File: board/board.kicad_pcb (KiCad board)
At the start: 2 copper layers, 58.1 x 29.5 mm, 41 parts, among them J2 Conn_01x10, J3 Conn_01x06, J4 Conn_01x02, J7 Conn_01x30, J8 USB_C_Receptacle_USB2.0_16P, J9 Conn_01x02, U2 nPM1300-QEAA, U3 MDBT50Q-P1MV2, U4 TVS_Array, Y1 32k Hz

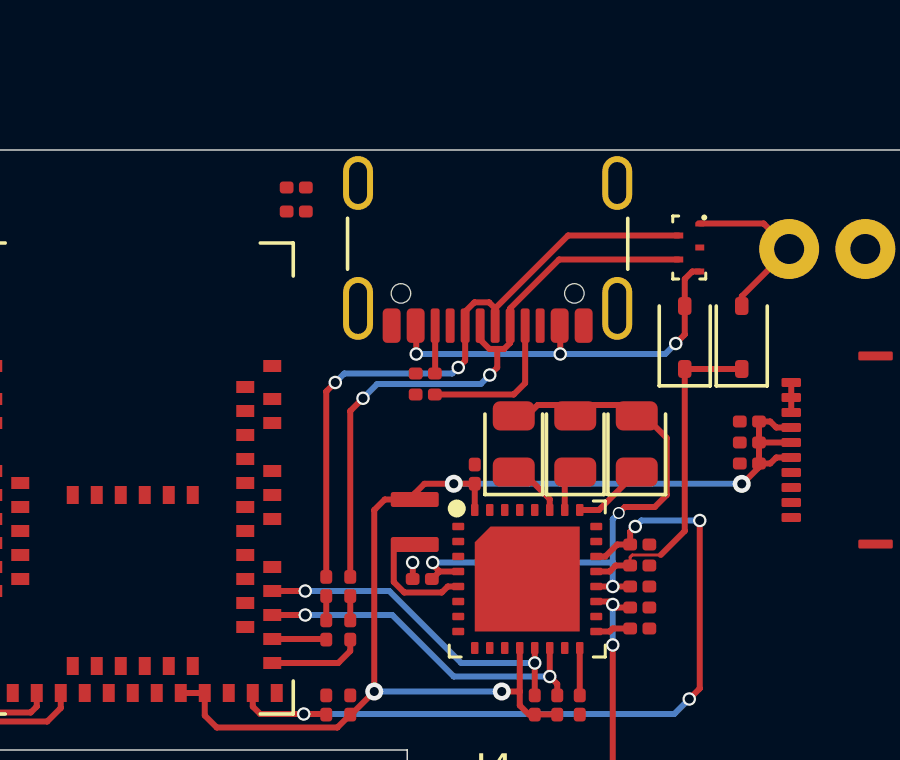
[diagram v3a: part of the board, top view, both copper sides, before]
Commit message: board: pcb add usb shield grounding
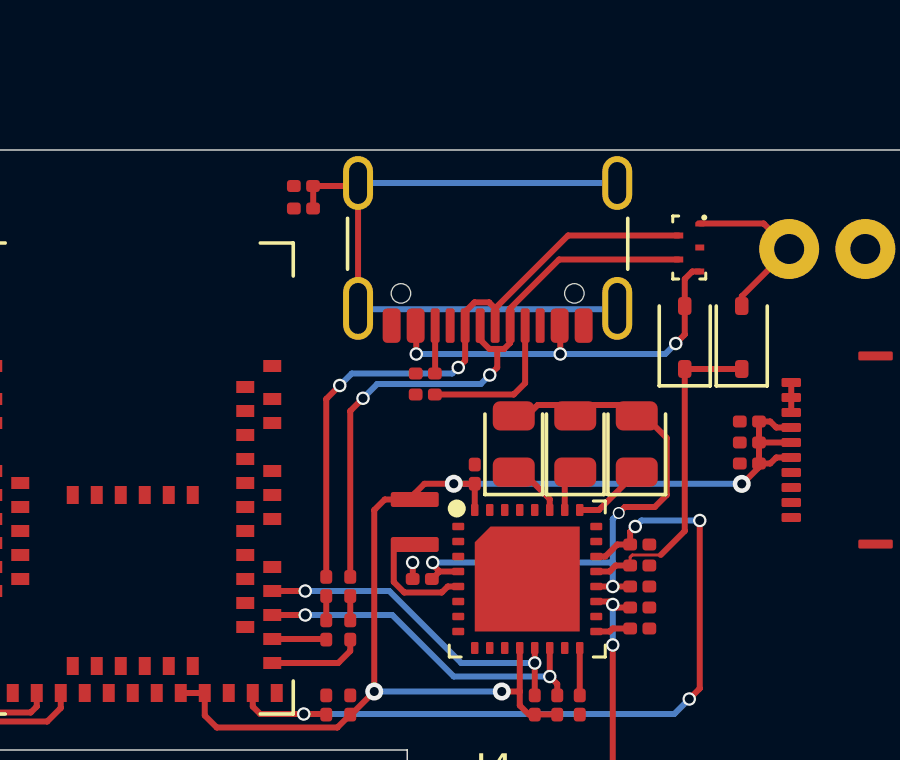
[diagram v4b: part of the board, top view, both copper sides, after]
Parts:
- moved C2 0.88 mm to (105.5, 48.2), turned to 0 degrees
- moved R5 0.74 mm to (105.5, 49.0), turned to 0 degrees
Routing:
- net Net-(J8-SHIELD): track 0.00 -> 23.8 mm
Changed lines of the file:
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@@
 	(footprint "Resistor_SMD:R_0201_0603Metric"
 		(layer "F.Cu")
-		(at 105.3 48.25 180)
+		(at 105.54 48.95)
 		(descr "Resistor SMD 0201 (0603 Metric), square (rectangular) end terminal, IPC-7351 nominal, (Body size source: https://www.vishay.com/docs/20052/crcw0201e3.pdf), generated with kicad-footprint-generator")
 		(tags "resistor")
@@
 		)
 		(property "LCSC PN" "C23024"
-			(at 0 0 180)
+			(at 0 0 0)
 			(unlocked yes)
 			(layer "F.Fab")
@@
 		(attr smd)
 		(fp_line
-			(start 0.7 0.35)
-			(end -0.7 0.35)
+			(start -0.7 -0.35)
+			(end 0.7 -0.35)
 			(stroke
 				(width 0.05)
@@
 		)
 		(fp_line
-			(start 0.7 -0.35)
-			(end 0.7 0.35)
+			(start -0.7 0.35)
+			(end -0.7 -0.35)
 			(stroke
 				(width 0.05)
@@
 		)
 		(fp_line
-			(start -0.7 0.35)
-			(end -0.7 -0.35)
+			(start 0.7 -0.35)
+			(end 0.7 0.35)
 			(stroke
 				(width 0.05)
@@
 		)
 		(fp_line
-			(start -0.7 -0.35)
-			(end 0.7 -0.35)
+			(start 0.7 0.35)
+			(end -0.7 0.35)
 			(stroke
 				(width 0.05)
@@
 		)
 		(fp_line
-			(start 0.3 0.15)
-			(end -0.3 0.15)
+			(start -0.3 -0.15)
+			(end 0.3 -0.15)
 			(stroke
 				(width 0.1)
@@
 		)
 		(fp_line
-			(start 0.3 -0.15)
-			(end 0.3 0.15)
+			(start -0.3 0.15)
+			(end -0.3 -0.15)
 			(stroke
 				(width 0.1)
@@
 		)
 		(fp_line
-			(start -0.3 0.15)
-			(end -0.3 -0.15)
+			(start 0.3 -0.15)
+			(end 0.3 0.15)
 			(stroke
 				(width 0.1)
@@
 		)
 		(fp_line
-			(start -0.3 -0.15)
-			(end 0.3 -0.15)
+			(start 0.3 0.15)
+			(end -0.3 0.15)
 			(stroke
 				(width 0.1)
@@
 		)
 		(fp_text user "${REFERENCE}"
-			(at -0.025 0.65 0)
+			(at -1.055 0 0)
 			(layer "F.Fab")
 			(effects
@@
 		)
 		(pad "" smd roundrect
-			(at -0.345 0 180)
+			(at -0.345 0)
 			(size 0.318 0.36)
 			(layers "F.Paste")
@@
 		)
 		(pad "" smd roundrect
-			(at 0.345 0 180)
+			(at 0.345 0)
 			(size 0.318 0.36)
 			(layers "F.Paste")
@@
 		)
 		(pad "1" smd roundrect
-			(at -0.32 0 180)
+			(at -0.32 0)
 			(size 0.46 0.4)
 			(layers "F.Cu" "F.Mask")
@@
 		)
 		(pad "2" smd roundrect
-			(at 0.32 0 180)
+			(at 0.32 0)
 			(size 0.46 0.4)
 			(layers "F.Cu" "F.Mask")
@@
 	(footprint "Capacitor_SMD:C_0201_0603Metric"
 		(layer "F.Cu")
-		(at 105.3 49.05 180)
+		(at 105.54 48.2)
 		(descr "Capacitor SMD 0201 (0603 Metric), square (rectangular) end terminal, IPC-7351 nominal, (Body size source: https://www.vishay.com/docs/20052/crcw0201e3.pdf), generated with kicad-footprint-generator")
 		(tags "capacitor")
@@
 		)
 		(property "LCSC PN" "C57112"
-			(at 0 0 180)
+			(at 0 0 0)
 			(unlocked yes)
 			(layer "F.Fab")
@@
 		(attr smd)
 		(fp_line
-			(start 0.7 0.35)
-			(end -0.7 0.35)
+			(start -0.7 -0.35)
+			(end 0.7 -0.35)
 			(stroke
 				(width 0.05)
@@
 		)
 		(fp_line
-			(start 0.7 -0.35)
-			(end 0.7 0.35)
+			(start -0.7 0.35)
+			(end -0.7 -0.35)
 			(stroke
 				(width 0.05)
@@
 		)
 		(fp_line
-			(start -0.7 0.35)
-			(end -0.7 -0.35)
+			(start 0.7 -0.35)
+			(end 0.7 0.35)
 			(stroke
 				(width 0.05)
@@
 		)
 		(fp_line
-			(start -0.7 -0.35)
-			(end 0.7 -0.35)
+			(start 0.7 0.35)
+			(end -0.7 0.35)
 			(stroke
 				(width 0.05)
@@
 		)
 		(fp_line
-			(start 0.3 0.15)
-			(end -0.3 0.15)
+			(start -0.3 -0.15)
+			(end 0.3 -0.15)
 			(stroke
 				(width 0.1)
@@
 		)
 		(fp_line
-			(start 0.3 -0.15)
-			(end 0.3 0.15)
+			(start -0.3 0.15)
+			(end -0.3 -0.15)
 			(stroke
 				(width 0.1)
@@
 		)
 		(fp_line
-			(start -0.3 0.15)
-			(end -0.3 -0.15)
+			(start 0.3 -0.15)
+			(end 0.3 0.15)
 			(stroke
 				(width 0.1)
@@
 		)
 		(fp_line
-			(start -0.3 -0.15)
-			(end 0.3 -0.15)
+			(start 0.3 0.15)
+			(end -0.3 0.15)
 			(stroke
 				(width 0.1)
@@
 		)
 		(fp_text user "${REFERENCE}"
-			(at 0 -0.68 0)
+			(at -1.005 0 0)
 			(layer "F.Fab")
 			(effects
@@
 		)
 		(pad "" smd roundrect
-			(at -0.345 0 180)
+			(at -0.345 0)
 			(size 0.318 0.36)
 			(layers "F.Paste")
@@
 		)
 		(pad "" smd roundrect
-			(at 0.345 0 180)
+			(at 0.345 0)
 			(size 0.318 0.36)
 			(layers "F.Paste")
@@
 		)
 		(pad "1" smd roundrect
-			(at -0.32 0 180)
+			(at -0.32 0)
 			(size 0.46 0.4)
 			(layers "F.Cu" "F.Mask")
@@
 		)
 		(pad "2" smd roundrect
-			(at 0.32 0 180)
+			(at 0.32 0)
 			(size 0.46 0.4)
 			(layers "F.Cu" "F.Mask")
@@
 	)
 	(segment
-		(start 106.6 54.75)
-		(end 106.3 55.05)
+		(start 106.75 54.85)
+		(end 106.3 55.3)
 		(width 0.2)
 		(layer "F.Cu")
@@
 	)
 	(segment
-		(start 106.3 55.05)
-		(end 106.3 61.235)
+		(start 111.93 52.280001)
+		(end 114.360001 49.85)
 		(width 0.2)
 		(layer "F.Cu")
@@
 	)
 	(segment
-		(start 111.93 52.280001)
-		(end 114.360001 49.85)
+		(start 111.728999 52.079)
+		(end 111.93 52.280001)
 		(width 0.2)
 		(layer "F.Cu")
@@
 	)
 	(segment
-		(start 111.728999 52.079)
-		(end 111.93 52.280001)
+		(start 106.3 55.3)
+		(end 106.3 61.235)
 		(width 0.2)
 		(layer "F.Cu")
@@
 	)
 	(via
-		(at 106.6 54.75)
+		(at 106.75 54.85)
 		(size 0.45)
 		(drill 0.3)
@@
 	)
 	(segment
-		(start 106.9 54.45)
+		(start 107.15 54.45)
 		(end 110.5 54.45)
 		(width 0.2)
@@
 	)
 	(segment
-		(start 110.5 54.45)
-		(end 110.7 54.25)
+		(start 106.75 54.85)
+		(end 107.15 54.45)
 		(width 0.2)
 		(layer "B.Cu")
@@
 	)
 	(segment
-		(start 106.6 54.75)
-		(end 106.9 54.45)
+		(start 110.5 54.45)
+		(end 110.7 54.25)
 		(width 0.2)
 		(layer "B.Cu")
@@
 	)
 	(segment
+		(start 105.865 48.2)
+		(end 107.255 48.2)
+		(width 0.2)
+		(layer "F.Cu")
+		(net 69)
+	)
+	(segment
+		(start 107.36 52.28)
+		(end 107.36 48.1)
+		(width 0.2)
+		(layer "F.Cu")
+		(net 69)
+	)
+	(segment
+		(start 105.865 48.95)
+		(end 105.865 48.2)
+		(width 0.2)
+		(layer "F.Cu")
+		(net 69)
+	)
+	(segment
+		(start 107.21 48.25)
+		(end 107.36 48.1)
+		(width 0.2)
+		(layer "F.Cu")
+		(net 69)
+	)
+	(segment
+		(start 116 52.28)
+		(end 115.974 52.306)
+		(width 0.2)
+		(layer "B.Cu")
+		(net 69)
+	)
+	(segment
+		(start 116 48.1)
+		(end 107.36 48.1)
+		(width 0.2)
+		(layer "B.Cu")
+		(net 69)
+	)
+	(segment
+		(start 115.974 52.306)
+		(end 107.386 52.306)
+		(width 0.2)
+		(layer "B.Cu")
+		(net 69)
+	)
+	(segment
+		(start 107.386 52.306)
+		(end 107.36 52.28)
+		(width 0.2)
+		(layer "B.Cu")
+		(net 69)
+	)
+	(segment

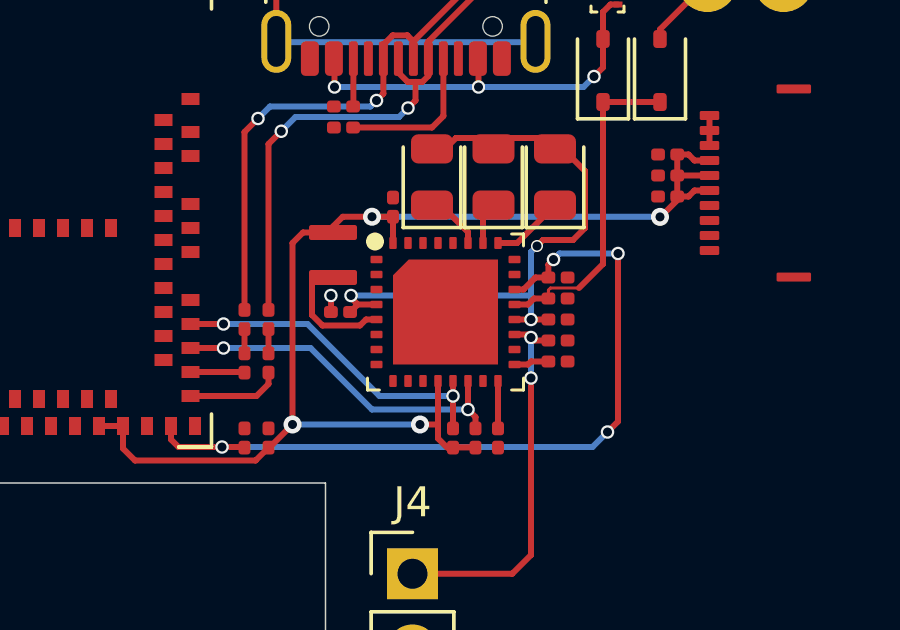
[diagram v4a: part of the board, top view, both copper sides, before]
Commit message: board: pcb route display spi
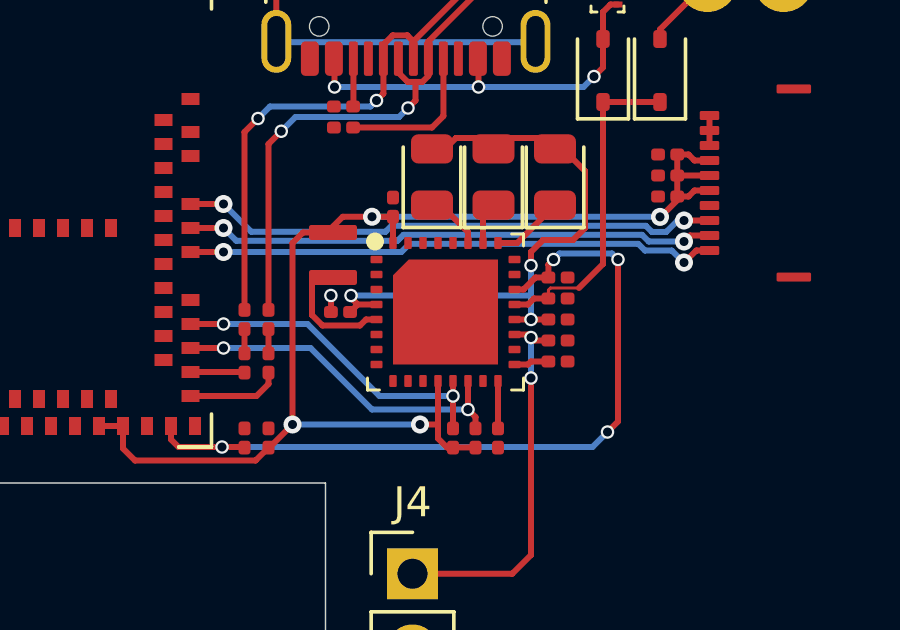
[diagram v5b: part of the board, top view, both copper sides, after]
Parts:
- R5: value 300kR -> 10kR
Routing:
- net scs: track 0.00 -> 18.0 mm, vias 0 -> 2
- net sclk: track 0.00 -> 17.8 mm, vias 0 -> 2
- net si: track 0.00 -> 17.7 mm, vias 0 -> 2

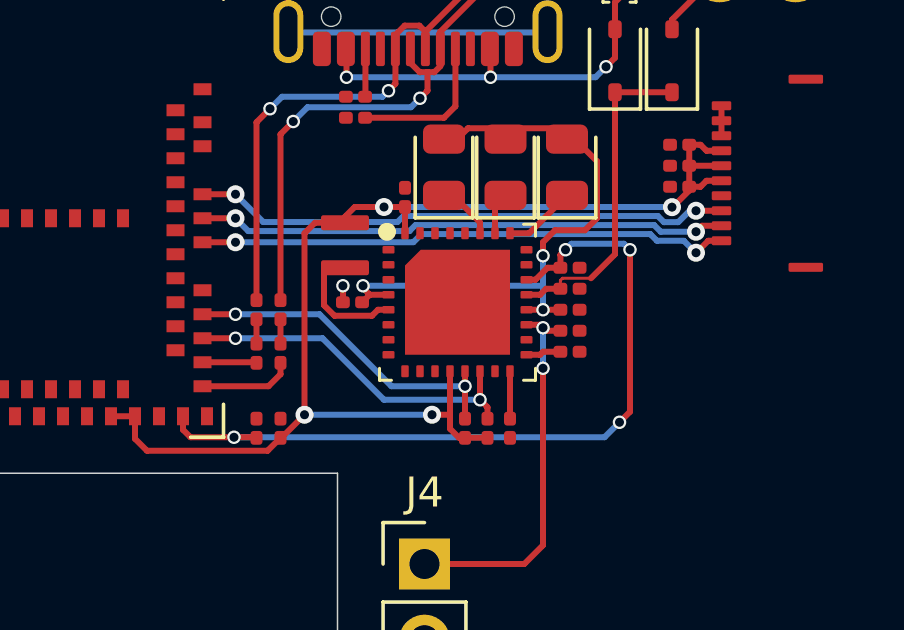
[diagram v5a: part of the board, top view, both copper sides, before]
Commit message: board: pcb optimize routing
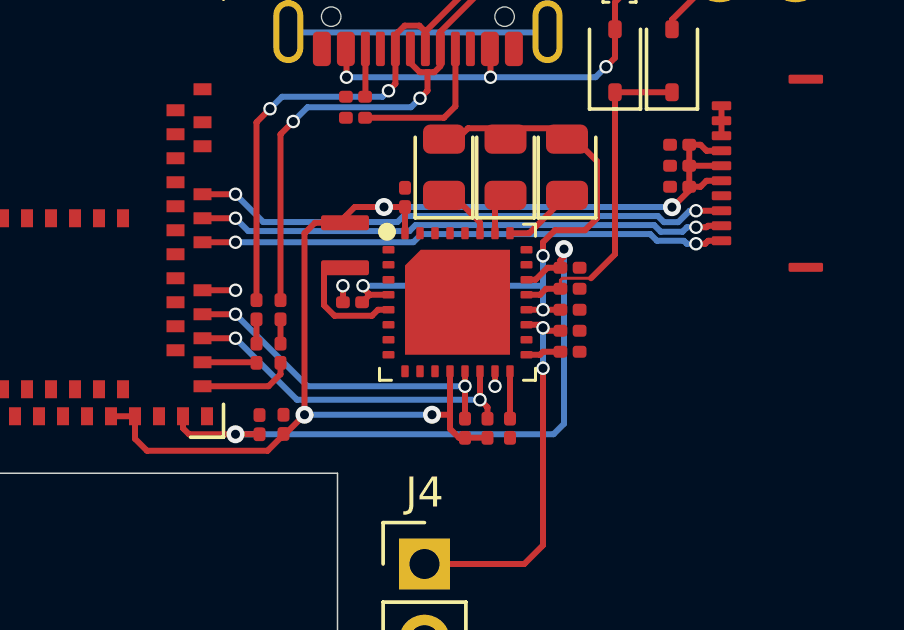
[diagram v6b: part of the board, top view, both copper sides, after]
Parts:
- moved C10 0.16 mm to (107.2, 65.4)
- moved C9 0.16 mm to (106.4, 65.4)
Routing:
- net vbus: track 26.3 -> 21.9 mm, vias 4 -> 2
- net shphld: track 0.00 -> 1.60 mm, vias 0 -> 2
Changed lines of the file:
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@@
 	(footprint "Capacitor_SMD:C_0201_0603Metric"
 		(layer "F.Cu")
-		(at 106.3 65.5 90)
+		(at 106.4 65.38 90)
 		(descr "Capacitor SMD 0201 (0603 Metric), square (rectangular) end terminal, IPC-7351 nominal, (Body size source: https://www.vishay.com/docs/20052/crcw0201e3.pdf), generated with kicad-footprint-generator")
 		(tags "capacitor")
@@
 	(footprint "Capacitor_SMD:C_0201_0603Metric"
 		(layer "F.Cu")
-		(at 107.1 65.5 -90)
+		(at 107.2 65.37 -90)
 		(descr "Capacitor SMD 0201 (0603 Metric), square (rectangular) end terminal, IPC-7351 nominal, (Body size source: https://www.vishay.com/docs/20052/crcw0201e3.pdf), generated with kicad-footprint-generator")
 		(tags "capacitor")
@@
 	)
 	(segment
-		(start 106.28 65.8)
-		(end 106.3 65.82)
-		(width 0.2)
-		(layer "F.Cu")
-		(net 3)
-	)
-	(segment
 		(start 115.6 60.55)
 		(end 116 60.15)
@@
 	)
 	(segment
-		(start 118.75 59.55)
-		(end 118.75 64.95)
+		(start 105.6 65.7)
+		(end 104.05 65.7)
 		(width 0.2)
 		(layer "F.Cu")
@@
 	)
 	(segment
-		(start 116.43 59.72)
-		(end 116.6 59.55)
+		(start 116.55 59.528)
+		(end 116.55 59.78)
 		(width 0.2)
 		(layer "F.Cu")
@@
 	)
 	(segment
-		(start 105.55 65.8)
-		(end 104.1 65.8)
+		(start 104.05 65.7)
+		(end 103.85 65.5)
 		(width 0.2)
 		(layer "F.Cu")
@@
 	)
 	(segment
-		(start 116.425 60.145)
-		(end 116.43 60.15)
+		(start 116.55 59.78)
+		(end 116.43 59.9)
 		(width 0.2)
 		(layer "F.Cu")
@@
 	)
 	(segment
-		(start 104.1 65.8)
-		(end 103.85 65.55)
+		(start 116.43 59.9)
+		(end 116.43 60.15)
 		(width 0.2)
 		(layer "F.Cu")
@@
 	)
 	(segment
-		(start 118.75 64.95)
-		(end 118.4 65.3)
+		(start 116.425 60.145)
+		(end 116.43 60.15)
 		(width 0.2)
 		(layer "F.Cu")
@@
 	)
 	(segment
-		(start 103.85 65.55)
+		(start 103.85 65.5)
 		(end 103.85 65.1)
 		(width 0.2)
@@
 	)
 	(segment
-		(start 116.43 60.15)
-		(end 116.43 59.72)
-		(width 0.2)
-		(layer "F.Cu")
-		(net 3)
-	)
-	(segment
-		(start 105.55 65.8)
-		(end 106.28 65.8)
+		(start 106.4 65.7)
+		(end 105.6 65.7)
 		(width 0.2)
 		(layer "F.Cu")
@@
 	)
 	(via
-		(at 118.75 59.55)
-		(size 0.45)
-		(drill 0.3)
-		(layers "F.Cu" "B.Cu")
-		(net 3)
-	)
-	(via
-		(at 116.6 59.55)
-		(size 0.45)
-		(drill 0.3)
-		(layers "F.Cu" "B.Cu")
-		(net 3)
-	)
-	(via
-		(at 105.55 65.8)
-		(size 0.45)
+		(at 116.55 59.528)
+		(size 0.6)
 		(drill 0.3)
 		(layers "F.Cu" "B.Cu")
@@
 	)
 	(via
-		(at 118.4 65.3)
-		(size 0.45)
+		(at 105.6 65.7)
+		(size 0.6)
 		(drill 0.3)
 		(layers "F.Cu" "B.Cu")
@@
 	)
 	(segment
-		(start 118.55 59.35)
-		(end 116.8 59.35)
+		(start 105.6 65.7)
+		(end 116.2 65.7)
 		(width 0.2)
 		(layer "B.Cu")
@@
 	)
 	(segment
-		(start 118.4 65.3)
-		(end 117.9 65.8)
+		(start 116.2 65.7)
+		(end 116.55 65.35)
 		(width 0.2)
 		(layer "B.Cu")
@@
 	)
 	(segment
-		(start 116.8 59.35)
-		(end 116.6 59.55)
-		(width 0.2)
-		(layer "B.Cu")
-		(net 3)
-	)
-	(segment
-		(start 117.9 65.8)
-		(end 105.55 65.8)
-		(width 0.2)
-		(layer "B.Cu")
-		(net 3)
-	)
-	(segment
-		(start 118.75 59.55)
-		(end 118.55 59.35)
+		(start 116.55 65.35)
+		(end 116.55 59.528)
 		(width 0.2)
 		(layer "B.Cu")
@@
 	)
 	(segment
-		(start 113.25 64.1)
-		(end 110.8 64.1)
-		(width 0.2)
-		(layer "B.Cu")
-		(net 18)
-	)
-	(segment
-		(start 108.4 61.7)
+		(start 108 64.1)
 		(end 105.6 61.7)
 		(width 0.2)
@@
 	)
 	(segment
-		(start 110.8 64.1)
-		(end 108.4 61.7)
+		(start 113.25 64.1)
+		(end 108 64.1)
 		(width 0.2)
 		(layer "B.Cu")
@@
 	)
 	(segment
-		(start 108.5 62.5)
+		(start 107.65 64.55)
 		(end 105.6 62.5)
 		(width 0.2)
@@
 	(segment
 		(start 113.75 64.55)
-		(end 110.55 64.55)
-		(width 0.2)
-		(layer "B.Cu")
-		(net 19)
-	)
-	(segment
-		(start 110.55 64.55)
-		(end 108.5 62.5)
+		(end 107.65 64.55)
 		(width 0.2)
 		(layer "B.Cu")
@@
 	)
 	(segment
-		(start 104.5 59.3)
-		(end 105.6 59.3)
+		(start 121.8 59.25)
+		(end 121.358524 59.25)
 		(width 0.2)
 		(layer "F.Cu")
@@
 	)
 	(segment
-		(start 121.358524 59.25)
-		(end 121.8 59.25)
+		(start 121.258518 59.350006)
+		(end 120.95 59.350006)
 		(width 0.2)
 		(layer "F.Cu")
@@
 	)
 	(segment
-		(start 120.958518 59.650006)
-		(end 121.358524 59.25)
+		(start 104.5 59.3)
+		(end 105.6 59.3)
 		(width 0.2)
 		(layer "F.Cu")
@@
 	)
 	(segment
-		(start 120.95 59.650006)
-		(end 120.958518 59.650006)
+		(start 121.358524 59.25)
+		(end 121.258518 59.350006)
 		(width 0.2)
 		(layer "F.Cu")
@@
 	)
 	(via
-		(at 120.95 59.650006)
-		(size 0.6)
+		(at 105.6 59.3)
+		(size 0.45)
 		(drill 0.3)
 		(layers "F.Cu" "B.Cu")
@@
 	)
 	(via
-		(at 105.6 59.3)
-		(size 0.6)
+		(at 120.95 59.350006)
+		(size 0.45)
 		(drill 0.3)
 		(layers "F.Cu" "B.Cu")
@@
 	)
 	(segment
-		(start 120.941482 59.650006)
-		(end 120.95 59.650006)
+		(start 120.95 59.350006)
+		(end 120.641482 59.350006)
 		(width 0.2)
 		(layer "B.Cu")
@@
 	)
 	(segment
-		(start 120.542479 59.251003)
-		(end 120.941482 59.650006)
+		(start 111.8 59.028)
+		(end 119.426 59.028)
 		(width 0.2)
 		(layer "B.Cu")
@@
 	(segment
 		(start 111.8 59.028)
-		(end 119.426 59.028)
+		(end 111.528 59.3)
 		(width 0.2)
 		(layer "B.Cu")
@@
 	)
 	(segment
-		(start 111.8 59.028)
-		(end 111.528 59.3)
+		(start 120.641482 59.350006)
+		(end 120.542479 59.251003)
 		(width 0.2)
 		(layer "B.Cu")
@@
 	)
 	(segment
+		(start 104.5 60.9)
+		(end 105.6 60.9)
+		(width 0.2)
+		(layer "F.Cu")
+		(net 35)
+	)
+	(segment
+		(start 114.25 63.6)
+		(end 114.25 64.1)
+		(width 0.2)
+		(layer "F.Cu")
+		(net 35)
+	)
+	(via
+		(at 114.25 64.1)
+		(size 0.45)
+		(drill 0.3)
+		(layers "F.Cu" "B.Cu")
+		(net 35)
+	)
+	(via
+		(at 105.6 60.9)
+		(size 0.45)
+		(drill 0.3)
+		(layers "F.Cu" "B.Cu")
+		(net 35)
+	)
+	(segment
 		(start 104.5 57.7)
 		(end 105.6 57.7)
@@
 	(via
 		(at 120.95 58.25)
-		(size 0.6)
+		(size 0.45)
 		(drill 0.3)
 		(layers "F.Cu" "B.Cu")
@@
 	(via
 		(at 105.6 57.7)
-		(size 0.6)
+		(size 0.45)
 		(drill 0.3)
 		(layers "F.Cu" "B.Cu")
@@
 	)
 	(segment
+		(start 120.950003 58.8)
+		(end 120.95 58.800003)
+		(width 0.2)
+		(layer "F.Cu")
+		(net 39)
+	)
+	(segment
 		(start 104.5 58.5)
 		(end 105.6 58.5)
@@
 	)
 	(segment
+		(start 121.35 58.75)
+		(end 121.3 58.8)
+		(width 0.2)
+		(layer "F.Cu")
+		(net 39)
+	)
+	(segment
 		(start 121.8 58.75)
-		(end 121.150003 58.75)
+		(end 121.35 58.75)
 		(width 0.2)
 		(layer "F.Cu")
@@
 	)
 	(segment
-		(start 121.150003 58.75)
-		(end 120.95 58.950003)
+		(start 121.3 58.8)
+		(end 120.950003 58.8)
 		(width 0.2)
 		(layer "F.Cu")
@@
 	)
 	(via
-		(at 120.95 58.950003)
-		(size 0.6)
+		(at 120.95 58.800003)
+		(size 0.45)
 		(drill 0.3)
 		(layers "F.Cu" "B.Cu")
@@
 	(via
 		(at 105.6 58.5)
-		(size 0.6)
+		(size 0.45)
 		(drill 0.3)
 		(layers "F.Cu" "B.Cu")
@@
 	)
 	(segment
-		(start 111.4 58.927)
+		(start 119.551322 58.727)
 		(end 111.6 58.727)
 		(width 0.2)
@@
 	)
 	(segment
-		(start 119.551322 58.727)
-		(end 119.774325 58.950003)
+		(start 120.65 58.8)
+		(end 120.499997 58.950003)
 		(width 0.2)
 		(layer "B.Cu")
@@
 	(segment
 		(start 111.6 58.727)
-		(end 119.551322 58.727)
+		(end 111.4 58.927)
 		(width 0.2)
 		(layer "B.Cu")
@@
 	(segment
 		(start 119.774325 58.950003)
-		(end 120.95 58.950003)
+		(end 119.551322 58.727)
 		(width 0.2)
 		(layer "B.Cu")
@@
 	)
 	(segment
-		(start 105.6 58.5)
-		(end 106.027 58.927)
+		(start 120.499997 58.950003)
+		(end 119.774325 58.950003)
+		(width 0.2)
+		(layer "B.Cu")
+		(net 39)
+	)
+	(segment
+		(start 120.949997 58.8)
+		(end 120.65 58.8)
 		(width 0.2)
 		(layer "B.Cu")
@@
 	(segment
 		(start 106.027 58.927)
-		(end 111.4 58.927)
+		(end 105.6 58.5)
+		(width 0.2)
+		(layer "B.Cu")
+		(net 39)
+	)
+	(segment
+		(start 111.4 58.927)
+		(end 106.027 58.927)
+		(width 0.2)
+		(layer "B.Cu")
+		(net 39)
+	)
+	(segment
+		(start 120.95 58.800003)
+		(end 120.949997 58.8)
 		(width 0.2)
 		(layer "B.Cu")
